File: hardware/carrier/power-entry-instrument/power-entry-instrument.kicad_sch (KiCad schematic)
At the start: 9 parts

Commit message: Main board: apply the chosen parts to every symbol and row
Every main-board and adapter symbol now carries Footprint, Manufacturer,
MPN, LCSC and Assembly. The values come from the selections whose
datasheets are banked. The BOM rows follow those choices:

- D-USBOR is the SS14 (SMA).
- J-LED is four solder pads, not a connector.
- L-BUCK-IN is 22 uH, C-BUCK-IN is a UCM electrolytic, C-STRIP-BULK is
  470 uF 25 V.
- D-TVS-BREATH is the PESD12VS1UA (SOD-323); the UB is SOD523.
- J-UMB is the hanxia header. Its posts go through the adapter and its
  tails through the tongue; the old wording had them swapped.
- U-BUCK and U-BREATH say where to buy.
- C-ADC-BULK is 1206 if fitted.

The body and geometry follow the chosen parts:

- The J-UMB and J-MCU envelopes in config/body.yaml are now read off the
  parts' drawings.
- J-MCU is longer, so the regulator block moved and the right-hand ribbon
  header followed it by 1.5 mm. The RH key board is re-laid out, with C8
  moving with the header's 3V3 pin. It checks clean.
- A mount candidate is now nudged by up to 3 mm before it is dropped. All
  seven main-board mounts hold.

New footprints and pages:

- New woody.pretty footprints: the MPXV4006DP (case 1351-01) from
  breath-sense-link.md's land pattern, and the NE8FAV from Neutrik's
  layout, mirrored to the top view.
- The input-LC derivation uses the chosen capacitor's banked ESR: Q is at
  most 1.8, and the margin is 120x worst case.
- The main-board README lists what is still open before layout.

Co-Authored-By: Claude Opus 5.5 <noreply@anthropic.com>
Claude-Session: https://claude.ai/code/session_01LmB4muFXnoLprWX4JzuJ5A
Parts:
- C-BUCK-IN: footprint (none) -> Capacitor_SMD:CP_Elec_6.3x5.8; Assembly (none) -> machine; LCSC (none) -> C729678; MPN (none) -> UCM1E101MCL1GS; Manufacturer (none) -> Nichicon
- C-STRIP-BULK: value 470-1000uF -> 470uF 25V; footprint (none) -> Capacitor_SMD:CP_Elec_10x10; Assembly (none) -> machine; LCSC (none) -> C340751; MPN (none) -> UCW1E471MNL1GS; Manufacturer (none) -> Nichicon
- D-REVSHUNT: footprint (none) -> Diode_SMD:D_SMC; Assembly (none) -> machine; LCSC (none) -> C13354; MPN (none) -> SS34-E3/57T; Manufacturer (none) -> Vishay General Semiconductor
- D-TVS-PWR: footprint (none) -> Diode_SMD:D_SMA; Assembly (none) -> machine; LCSC (none) -> C148216; MPN (none) -> SMAJ15A; Manufacturer (none) -> Littelfuse
- D-USBOR-A: value 1N5817 (DO-41) or SS14 (SMA) -> SS14; footprint (none) -> Diode_SMD:D_SMA; Assembly (none) -> machine; LCSC (none) -> C47460; MPN (none) -> SS14-E3/61T; Manufacturer (none) -> Vishay
- L-BUCK-IN: value 10-47uH -> 22uH; footprint (none) -> Inductor_SMD:L_Sunlord_SWPA6028S; Assembly (none) -> machine; LCSC (none) -> C51349; MPN (none) -> SWPA6028S220MT; Manufacturer (none) -> Sunlord
- NT-AGND: footprint (none) -> NetTie:NetTie-2_SMD_Pad0.5mm; Assembly (none) -> none
- U-BUCK-A: footprint (none) -> Converter_DCDC:Converter_DCDC_RECOM_R-78E-0.5_THT; Assembly (none) -> hand; LCSC (none) -> C3033024; MPN (none) -> R-78E5.0-1.0; Manufacturer (none) -> Recom

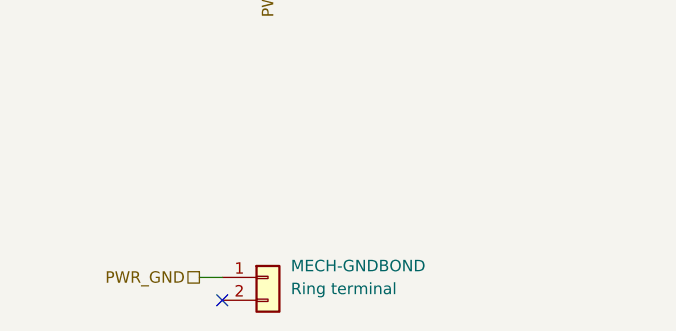
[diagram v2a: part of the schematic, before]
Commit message: Retire MECH-GNDBOND: the key plate grounds at one left-hand key-board mount
The owner approved this. MECH-GNDBOND (a ring terminal, a wire and M3
hardware from the main board) is removed from the power-entry sheet, its BOM
row and every page that named it.

- ADR 0020 Amendment 5: the key plate bonds at one plated mount of the
  left-hand key board. That mount's GND_CHAIN is PWR_GND down the ribbon.
  It is the only bond, and every other key-board mount stays NPTH.
- PLATE-TOP: order it un-anodised, or mask round that stud; meter it at
  bring-up.
- The pages that described the old bond now describe the new one:
  power-entry-instrument.md, nets.yaml, carrier.md, cluster-boards.md,
  ks33-geometry.md, ADR 0022 and the main-board README.

The left-hand board's re-layout with its bonded mount (layout.yaml
bond_mount) is still being done and lands in the next commit.

Co-Authored-By: Claude Opus 5.5 <noreply@anthropic.com>
Claude-Session: https://claude.ai/code/session_01LmB4muFXnoLprWX4JzuJ5A
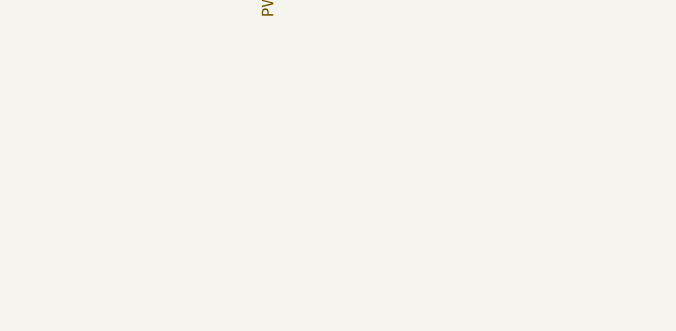
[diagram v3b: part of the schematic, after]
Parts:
- removed MECH-GNDBOND: Ring terminal, symbol Connector_Generic:Conn_01x02
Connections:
- no-connect marks 1 -> 0
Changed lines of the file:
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@@
     (instances (project "main-board" (path "/b12a49ac-ffa0-5078-b2ba-e15d161f1936/4727eca5-0a6b-5761-98ac-51ca9f544ea2" (reference "NT2") (unit 1))) (project "power-entry-instrument" (path "/ba12e546-d582-5654-bb26-6a94a8f78514" (reference "NT-AGND") (unit 1))))
-  )
-  (symbol (lib_id "Connector_Generic:Conn_01x02") (at 40.64 142.24 0) (unit 1)
-    (in_bom yes) (on_board yes) (dnp no)
-    (property "Reference" "MECH-GNDBOND" (at 43.18 140.97 0) (effects (font (size 1.27 1.27)) (justify left)))
-    (property "Value" "Ring terminal" (at 43.18 143.51 0) (effects (font (size 1.27 1.27)) (justify left)))
-    (property "Footprint" "" (at 40.64 142.24 0) (effects (font (size 1.27 1.27)) hide))
-    (property "Datasheet" "" (at 40.64 142.24 0) (effects (font (size 1.27 1.27)) hide))
-    (property "Row" "MECH-GNDBOND" (at 40.64 142.24 0) (effects (font (size 1.27 1.27)) hide))
-    (property "Pins" "1=1 2=2" (at 40.64 142.24 0) (effects (font (size 1.27 1.27)) hide))
-    (property "Note" "THE ALUMINIUM KEY PLATE BONDS TO PWR_GND, NEVER TO AGND, and this board is the only place that bond can originate" (at 40.64 142.24 0) (effects (font (size 1.27 1.27)) hide))
-    (property "Pins_source" "the ring terminal's two ends: 1 the board's ground pad, 2 the plate" (at 40.64 142.24 0) (effects (font (size 1.27 1.27)) hide))
-    (pin "1")
-    (pin "2")
-    (instances (project "main-board" (path "/b12a49ac-ffa0-5078-b2ba-e15d161f1936/4727eca5-0a6b-5761-98ac-51ca9f544ea2" (reference "E1") (unit 1))) (project "power-entry-instrument" (path "/ba12e546-d582-5654-bb26-6a94a8f78514" (reference "MECH-GNDBOND") (unit 1))))
   )
   (wire (pts (xy 36.83 50.8) (xy 34.29 50.8)) (stroke (width 0) (type default)))
@@
     (property "From" "module/power-entry" (at 91.44 106.68 0) (effects (font (size 1.27 1.27)) hide))
     (property "Figure" "umbilical-pinmap" (at 91.44 106.68 0) (effects (font (size 1.27 1.27)) hide)))
-  (wire (pts (xy 35.56 142.24) (xy 33.02 142.24)) (stroke (width 0) (type default)))
-  (hierarchical_label "PWR_GND" (shape passive) (at 33.02 142.24 180) (effects (font (size 1.27 1.27)) (justify right))
-    (property "Dir" "ref" (at 33.02 142.24 0) (effects (font (size 1.27 1.27)) hide))
-    (property "From" "module/power-entry" (at 33.02 142.24 0) (effects (font (size 1.27 1.27)) hide))
-    (property "Figure" "umbilical-pinmap" (at 33.02 142.24 0) (effects (font (size 1.27 1.27)) hide)))
   (wire (pts (xy 195.58 96.52) (xy 198.12 96.52)) (stroke (width 0) (type default)))
   (hierarchical_label "PWR_GND" (shape passive) (at 198.12 96.52 0) (effects (font (size 1.27 1.27)) (justify left))
@@
     (property "From" "carrier/power-entry-instrument" (at 187.96 96.52 0) (effects (font (size 1.27 1.27)) hide))
     (property "Figure" "dig-gnd-topology" (at 187.96 96.52 0) (effects (font (size 1.27 1.27)) hide)))
-  (no_connect (at 35.56 144.78))
   (text "Supplied by other circuits (PWR_FLAG):" (at 40.64 20.32 0) (effects (font (size 1.27 1.27)) (justify left top)))
   (symbol (lib_id "power:+12V") (at 43.18 30.48 0) (unit 1)

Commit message: Four-layer main-board ground written; breath clamps to the PWR_GND plane
power-entry-instrument.md section 2: layer 2 is the PWR_GND plane under every
SPI/chain/LED trace; AGND_INST is an island under the analog block, tied by
NT-AGND under U-ADC; the breath pair crosses as a pair (AGND_SENSE Kelvin at
the sensor). D-TVS-BREATH anodes move from AGND_INST to PWR_GND (sheet, board,
nets.yaml). dig-gnd-topology stays disputed: its dispute is the MODULE board,
whose layer count is the owner's; a four-layer proposal is recorded on it.

Co-Authored-By: Claude Opus 5.5 <noreply@anthropic.com>
Claude-Session: https://claude.ai/code/session_01LmB4muFXnoLprWX4JzuJ5A
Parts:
- NT-AGND: Note The analog star's single tie to PWR_GND (carrier.md section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 -> The analog star's single tie to PWR_GND: copper only, under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
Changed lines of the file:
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@@
     (property "Row" "NT-AGND" (at 193.04 96.52 0) (effects (font (size 1.27 1.27)) hide))
     (property "Pins" "1=1 2=2" (at 193.04 96.52 0) (effects (font (size 1.27 1.27)) hide))
-    (property "Note" "The analog star's single tie to PWR_GND (carrier.md section 2, dig-gnd-topology): copper only, at the star" (at 193.04 96.52 0) (effects (font (size 1.27 1.27)) hide))
+    (property "Note" "The analog star's single tie to PWR_GND: copper only, under U-ADC between its VSS and its digital pins (power-entry-instrument.md section 2)" (at 193.04 96.52 0) (effects (font (size 1.27 1.27)) hide))
     (property "Pins_source" "a net tie's two pads: 1 the analog star, 2 PWR_GND" (at 193.04 96.52 0) (effects (font (size 1.27 1.27)) hide))
     (property "Manufacturer" "" (at 193.04 96.52 0) (effects (font (size 1.27 1.27)) hide))

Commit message: ADR 0028: the lights are thirteen LEDs on the main board; pages follow
New ADR 0028 (owner's decisions: 13 x WS2815B-V1, 12 V, backup chained,
100 nF each, white mask) with dated notes in 0014, 0016 and 0005. New
tracked figure led-row-current (170-195 mA, blocked on E6), owned by
led-strip-drive.md. Strip wording follows in carrier.md,
power-entry-instrument (page, and C-STRIP-BULK's Note on its sheet),
nets.yaml, the main board README (white mask, LED places), key-chain-loom,
breath-sense-link, firmware README and hardware/lib/README.

Co-Authored-By: Claude Opus 5.5 <noreply@anthropic.com>
Claude-Session: https://claude.ai/code/session_01LmB4muFXnoLprWX4JzuJ5A
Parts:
- C-STRIP-BULK: Note At the J-LED feed point. Bulk belongs where the current swi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 -> At the LED row's 12 V feed end. Bulk belongs where the curr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
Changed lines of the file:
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@@
     (property "Row" "C-STRIP-BULK" (at 142.24 50.8 0) (effects (font (size 1.27 1.27)) hide))
     (property "Pins" "1=1 2=2" (at 142.24 50.8 0) (effects (font (size 1.27 1.27)) hide))
-    (property "Note" "At the J-LED feed point. Bulk belongs where the current swings, and the swing is at the strip. One strip (ADR 0016)" (at 142.24 50.8 0) (effects (font (size 1.27 1.27)) hide))
+    (property "Note" "At the LED row's 12 V feed end. Bulk belongs where the current swings: the row's PWM steps its whole current at once, and each LED's own 100 nF (C-LED) takes only the edges (ADR 0028)" (at 142.24 50.8 0) (effects (font (size 1.27 1.27)) hide))
     (property "Pins_source" "pin 1 is the positive terminal" (at 142.24 50.8 0) (effects (font (size 1.27 1.27)) hide))
     (property "Manufacturer" "Nichicon" (at 142.24 50.8 0) (effects (font (size 1.27 1.27)) hide))

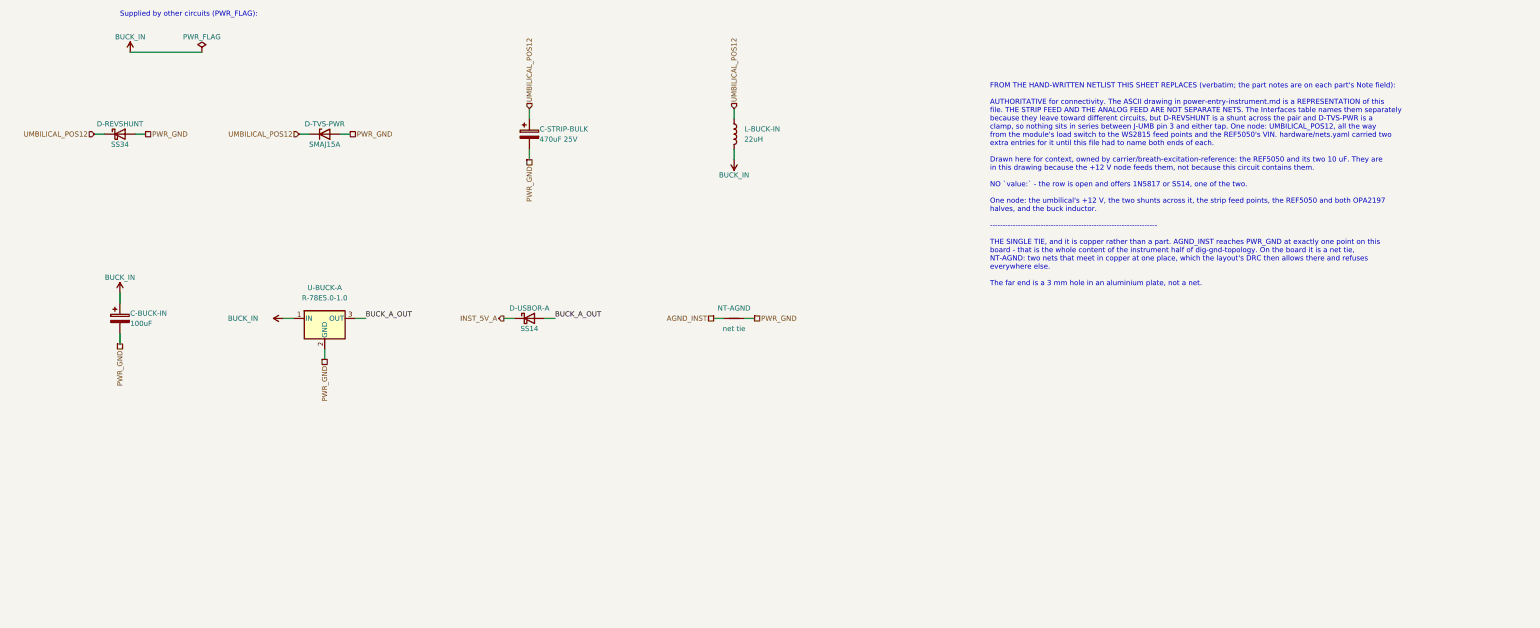
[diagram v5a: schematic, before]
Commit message: Instrument power entry: Q-INRUSH soft start between the connector and the bulk (sheets, WIP)
Q-INRUSH (AO3401A) and its gate network on the power-entry-instrument sheet;
the switched side is INST_POS12, which the LED drive and the analog reference
now receive. Exported; main board ERC clean. BOM, nets, sims and pages follow.

Co-Authored-By: Claude Opus 5.5 <noreply@anthropic.com>
Claude-Session: https://claude.ai/code/session_01LmB4muFXnoLprWX4JzuJ5A
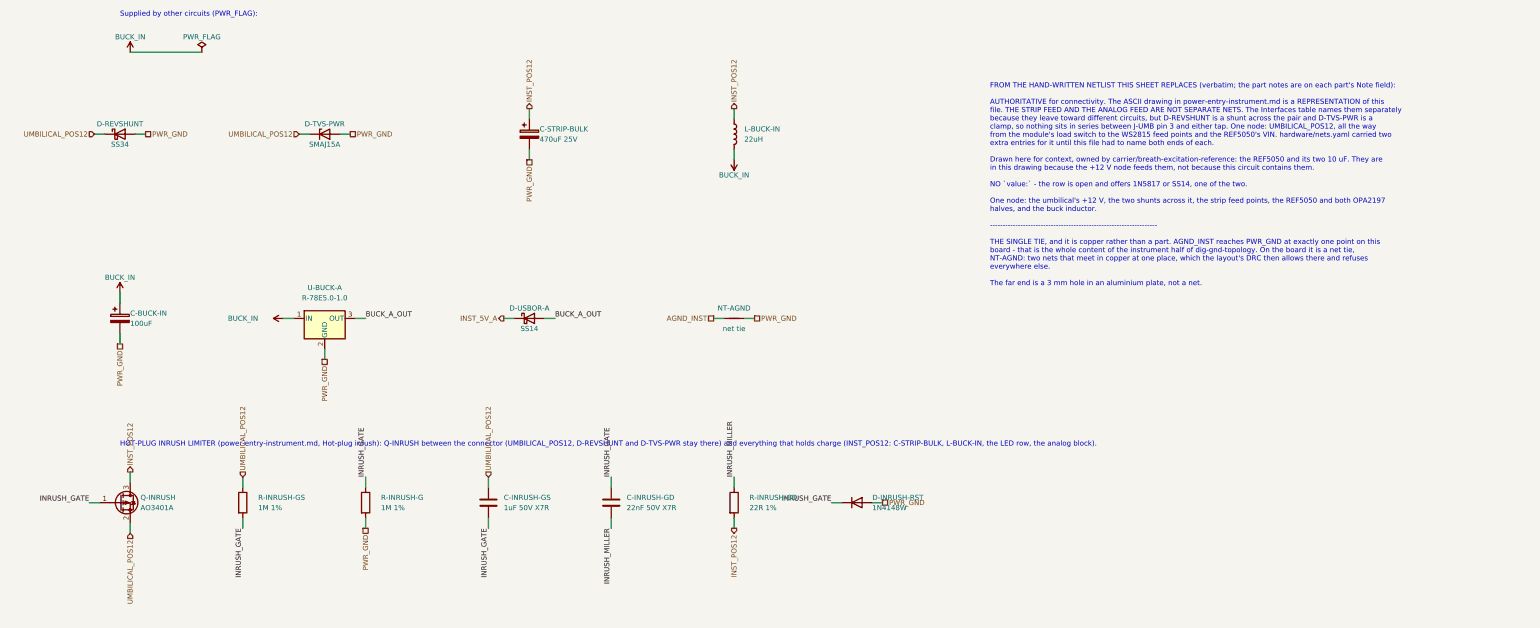
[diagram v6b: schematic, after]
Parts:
- added C-INRUSH-GD: 22nF 50V X7R, Capacitor_SMD:C_0805_2012Metric, symbol Device:C
- added C-INRUSH-GS: 1uF 50V X7R, Capacitor_SMD:C_0805_2012Metric, symbol Device:C
- added D-INRUSH-RST: 1N4148W, Diode_SMD:D_SOD-123, symbol Diode:1N4148W
- added Q-INRUSH: AO3401A, Package_TO_SOT_SMD:SOT-23, symbol Transistor_FET:AO3401A
- added R-INRUSH-G, R-INRUSH-GS: 1M 1%, Resistor_SMD:R_0805_2012Metric, symbol Device:R
- added R-INRUSH-GD: 22R 1%, Resistor_SMD:R_0805_2012Metric, symbol Device:R
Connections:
- net PWR_GND: now also D-INRUSH-RST.2 (A), R-INRUSH-G.2
- net UMBILICAL_POS12: now also C-INRUSH-GS.1, Q-INRUSH.2 (S), R-INRUSH-GS.1; no longer C-STRIP-BULK.1, L-BUCK-IN.1
- new net INRUSH_GATE: C-INRUSH-GD.1, C-INRUSH-GS.2, D-INRUSH-RST.1 (K), Q-INRUSH.1 (G), R-INRUSH-G.1, R-INRUSH-GS.2
- new net INRUSH_MILLER: C-INRUSH-GD.2, R-INRUSH-GD.1
- new net INST_POS12: C-STRIP-BULK.1, L-BUCK-IN.1, Q-INRUSH.3 (D), R-INRUSH-GD.2
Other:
- note added: "HOT-PLUG INRUSH LIMITER (power-entry-instrument.md, Hot-plug inrush): Q-INRUSH between the connector (UMBILICAL_POS12, D-REVSHUNT and D-TVS-PWR stay there) and everything that holds charge (INST_POS12: C-STRIP-BULK, L-BUCK-IN, the LED row, the analog block)."

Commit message: Bank the AO3401A and the 1N4148W (C81598); manifest rows for the inrush limiter's passives
Co-Authored-By: Claude Opus 5.5 <noreply@anthropic.com>
Claude-Session: https://claude.ai/code/session_01LmB4muFXnoLprWX4JzuJ5A
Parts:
- D-INRUSH-RST: Pins_source datasheets/discrete-and-power/1N4148W.pdf: SOD-123, cathode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 -> datasheets/discrete-and-power/SEMTECH-1N4148W-SOD123.pdf p.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
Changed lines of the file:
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@@
     (property "Pins" "K=1(K) A=2(A)" (at 223.52 142.24 0) (effects (font (size 1.27 1.27)) hide))
     (property "Note" "Resets the gate after an unplug: C-INRUSH-GS keeps V_GS while the instrument's capacitors drain, so the gate would be left below ground; this clamps it to -0.4 V, so once the input has fallen the next plug-in starts from off" (at 223.52 142.24 0) (effects (font (size 1.27 1.27)) hide))
-    (property "Pins_source" "datasheets/discrete-and-power/1N4148W.pdf: SOD-123, cathode band; KiCad pin 1 cathode" (at 223.52 142.24 0) (effects (font (size 1.27 1.27)) hide))
+    (property "Pins_source" "datasheets/discrete-and-power/SEMTECH-1N4148W-SOD123.pdf p.1 Pinning: pin 1 cathode, pin 2 anode (SOD-123); KiCad pin 1 cathode" (at 223.52 142.24 0) (effects (font (size 1.27 1.27)) hide))
     (property "Manufacturer" "ST(Semtech)" (at 223.52 142.24 0) (effects (font (size 1.27 1.27)) hide))
     (property "MPN" "1N4148W" (at 223.52 142.24 0) (effects (font (size 1.27 1.27)) hide))
